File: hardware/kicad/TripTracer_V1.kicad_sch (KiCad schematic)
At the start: 0 parts

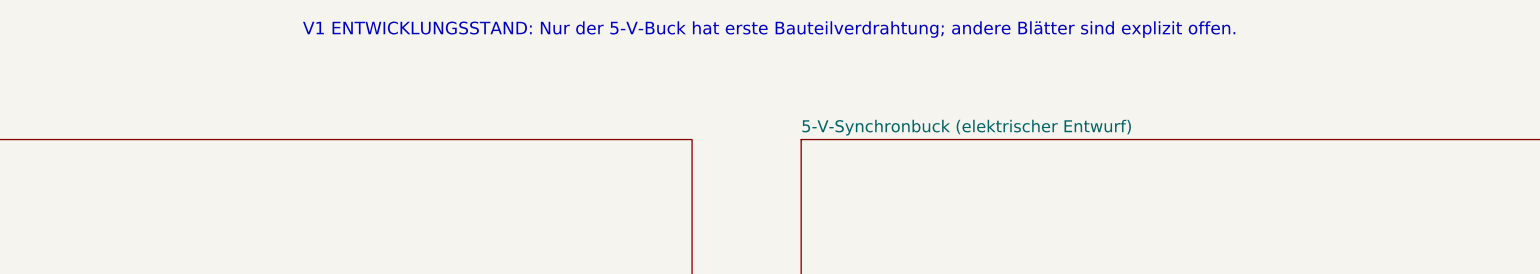
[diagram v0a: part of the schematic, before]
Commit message: hardware: mark V1 root with updated buck and MCU/USB implementation status
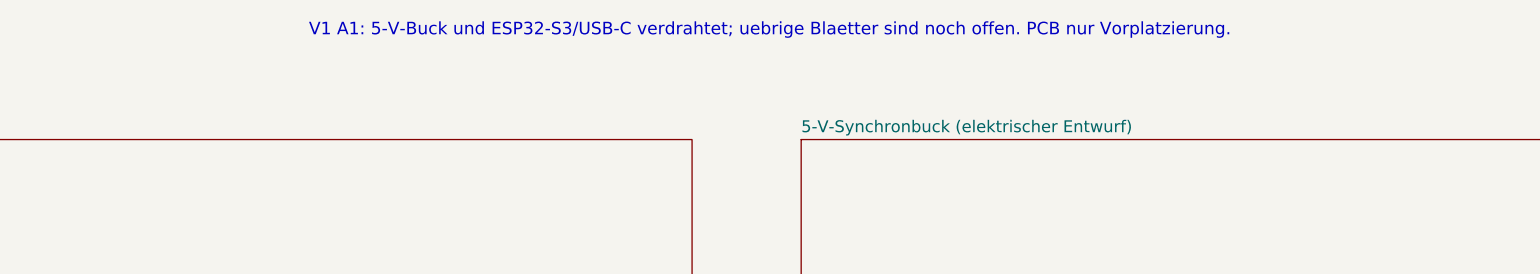
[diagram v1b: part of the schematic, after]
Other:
- note added: "V1 A1: 5-V-Buck und ESP32-S3/USB-C verdrahtet; uebrige Blaetter sind noch offen. PCB nur Vorplatzierung."
- note removed: "V1 ENTWICKLUNGSSTAND: Nur der 5-V-Buck hat erste Bauteilverdrahtung; andere Blätter sind explizit offen."
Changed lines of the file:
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@@
  (paper "A3")
  (title_block (title "TripTracer – Hardware V1 (Entwurf)") (date "2026-10-13") (rev "V1.0-a0 / NICHT FERTIGUNGSREIF") (company "TripTracer"))
- (text "V1 ENTWICKLUNGSSTAND: Nur der 5-V-Buck hat erste Bauteilverdrahtung; andere Blätter sind explizit offen." (at 210 16 0) (effects (font (size 1.6 1.6))))
+ (text "V1 A1: 5-V-Buck und ESP32-S3/USB-C verdrahtet; uebrige Blaetter sind noch offen. PCB nur Vorplatzierung." (at 210 16 0) (effects (font (size 1.6 1.6))))
  (sheet (at 25 30) (size 175 37) (exclude_from_sim no) (in_bom yes) (on_board yes) (dnp no)
  (stroke (width 0) (type solid)) (fill (color 0 0 0 0))

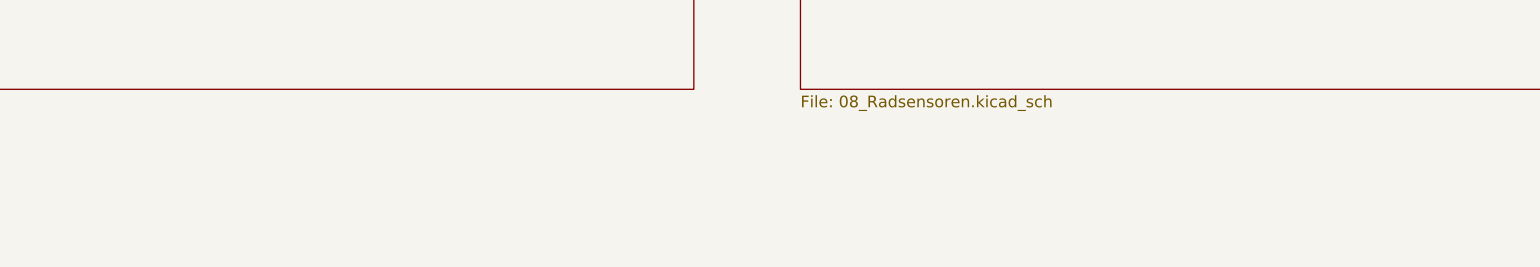
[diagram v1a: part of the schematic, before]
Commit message: hardware: annotate root schematic with single-project hierarchy navigation hint
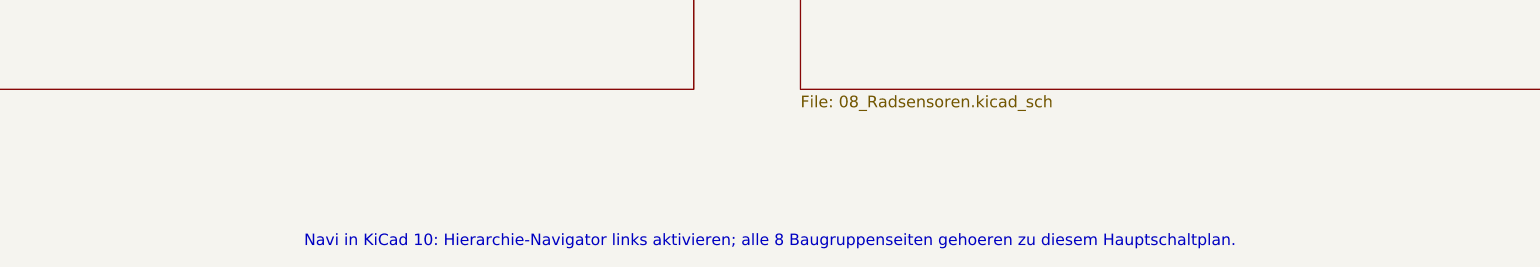
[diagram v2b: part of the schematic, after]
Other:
- note added: "Navi in KiCad 10: Hierarchie-Navigator links aktivieren; alle 8 Baugruppenseiten gehoeren zu diesem Hauptschaltplan."
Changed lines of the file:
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@@
  (property "Sheetfile" "08_Radsensoren.kicad_sch" (at 214 232.76 0) (effects (font (size 1.524 1.524)) (justify left top)))
  (instances (project "TripTracer_V1" (path "/a26d9b0c-7f10-4e5a-a65f-000000000064" (page "9")))))
+ (text "Navi in KiCad 10: Hierarchie-Navigator links aktivieren; alle 8 Baugruppenseiten gehoeren zu diesem Hauptschaltplan." (at 210 252 0) (effects (font (size 1.5 1.5))))
  (sheet_instances (path "/" (page "1")))
  (embedded_fonts no)

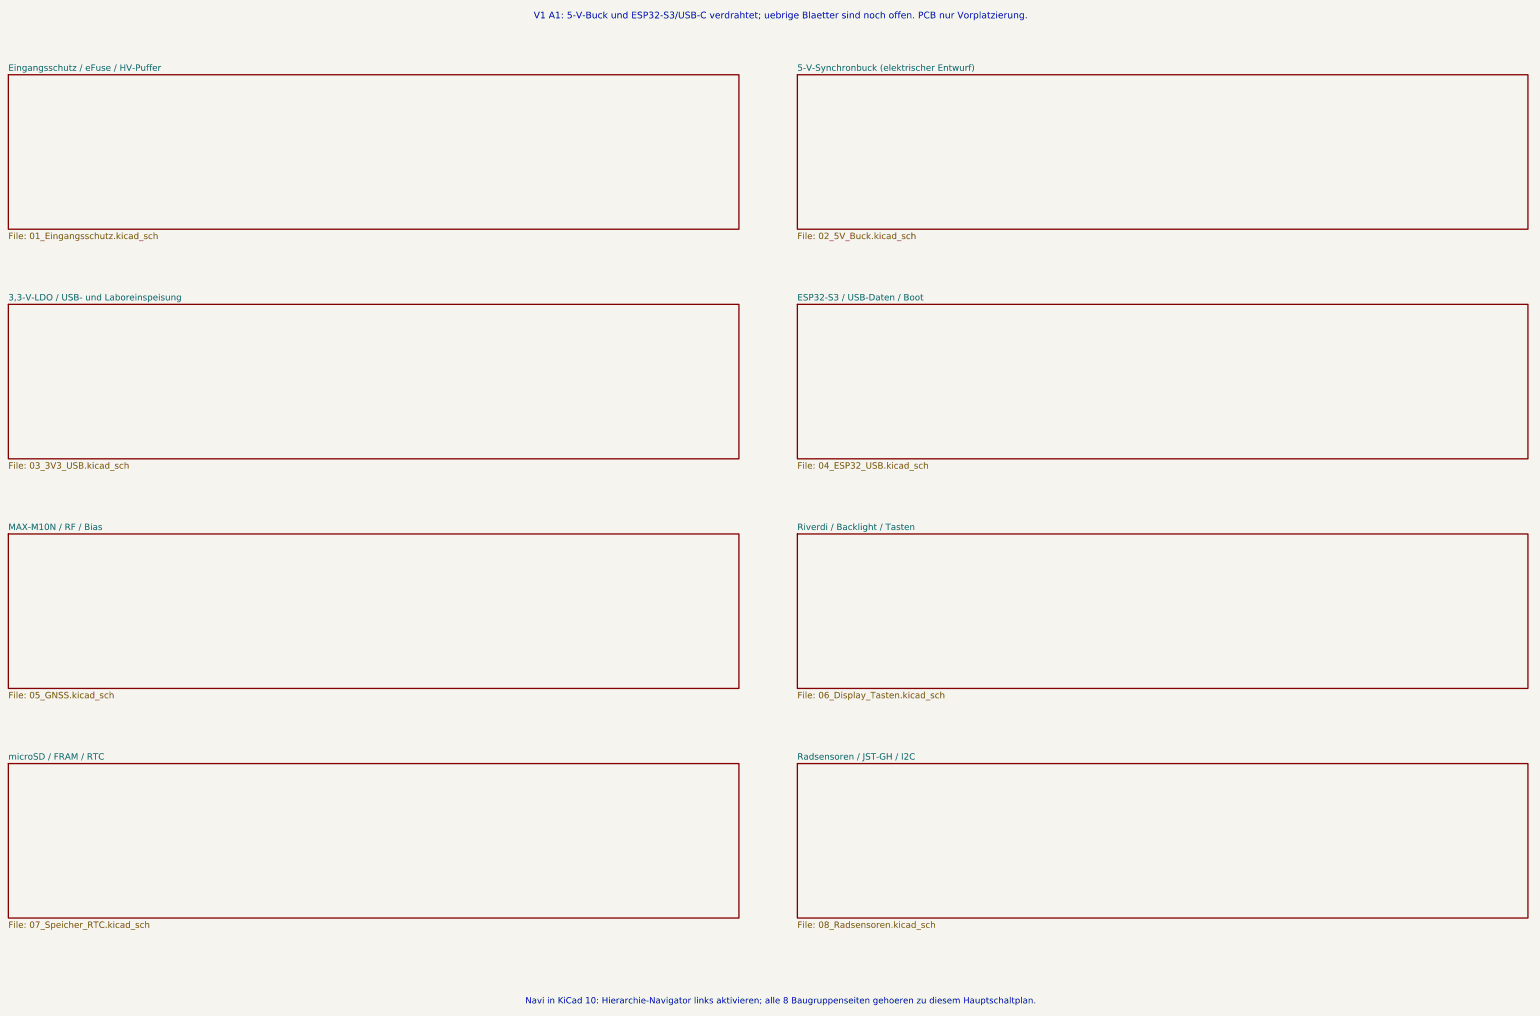
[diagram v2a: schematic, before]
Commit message: fix(kicad): align root hierarchy to connection grid without changing power nets
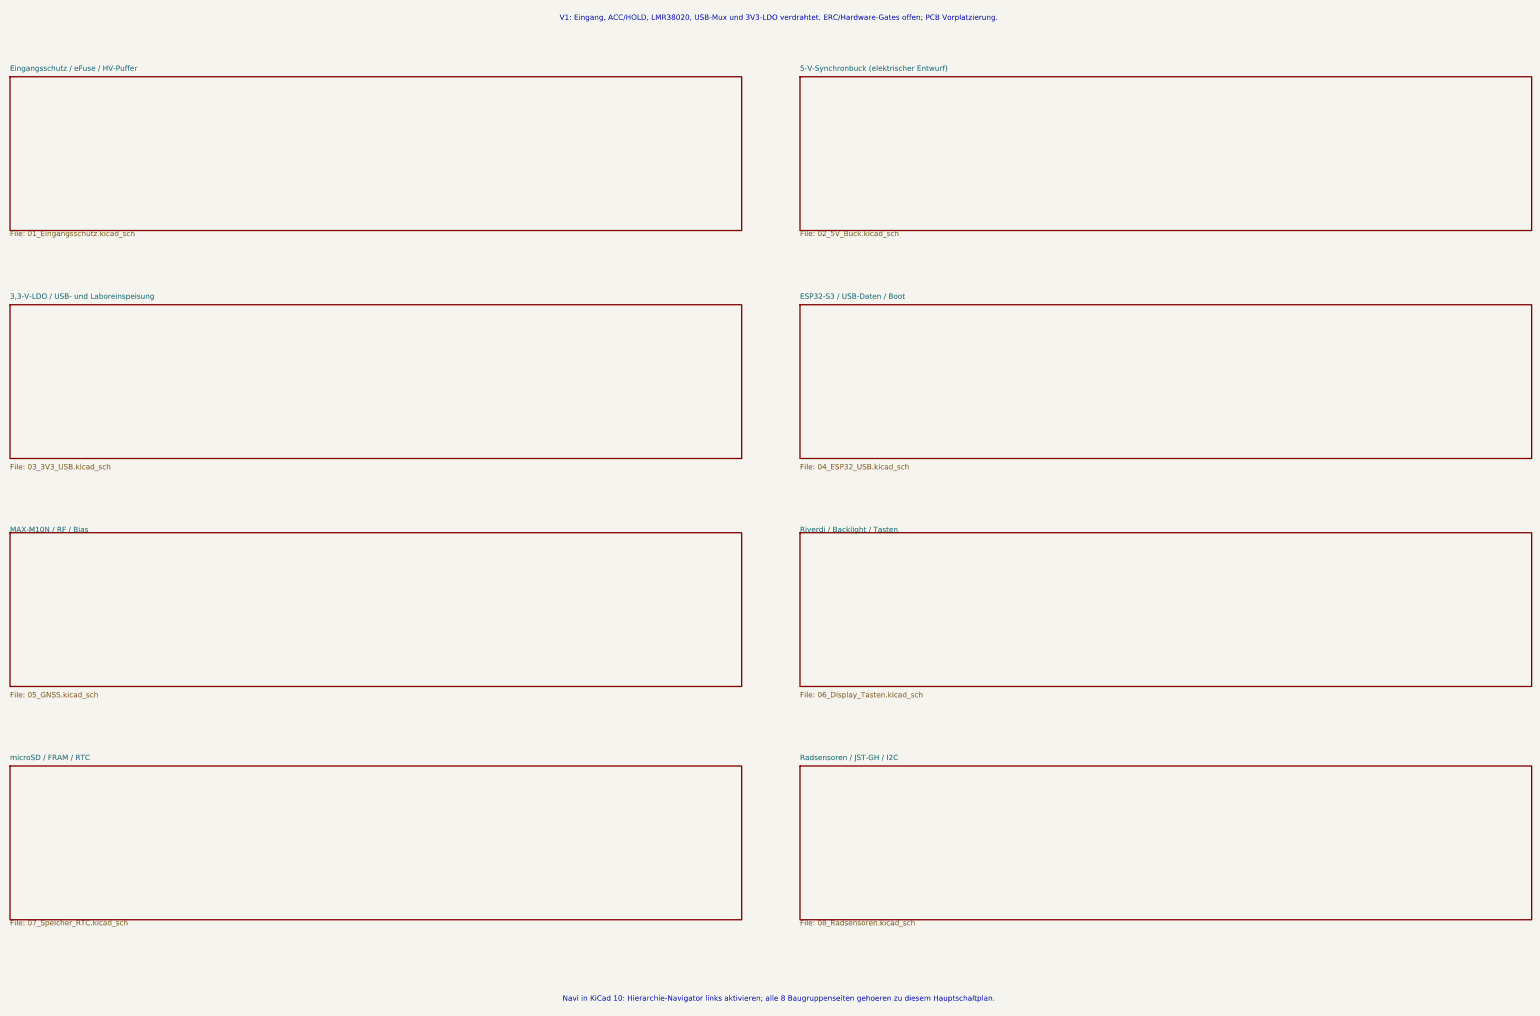
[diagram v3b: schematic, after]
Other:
- note added: "V1: Eingang, ACC/HOLD, LMR38020, USB-Mux und 3V3-LDO verdrahtet. ERC/Hardware-Gates offen; PCB Vorplatzierung."
- note removed: "V1 A1: 5-V-Buck und ESP32-S3/USB-C verdrahtet; uebrige Blaetter sind noch offen. PCB nur Vorplatzierung."
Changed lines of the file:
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@@
  (paper "A3")
  (title_block (title "TripTracer – Hardware V1 (Entwurf)") (date "2026-10-13") (rev "V1.0-a0 / NICHT FERTIGUNGSREIF") (company "TripTracer"))
- (text "V1 A1: 5-V-Buck und ESP32-S3/USB-C verdrahtet; uebrige Blaetter sind noch offen. PCB nur Vorplatzierung." (at 210 16 0) (effects (font (size 1.6 1.6))))
- (sheet (at 25 30) (size 175 37) (exclude_from_sim no) (in_bom yes) (on_board yes) (dnp no)
+ (text "V1: Eingang, ACC/HOLD, LMR38020, USB-Mux und 3V3-LDO verdrahtet. ERC/Hardware-Gates offen; PCB Vorplatzierung." (at 209.55 16.51 0) (effects (font (size 1.27 1.27))))
+ (sheet (at 25.4 30.48) (size 175.26 36.83) (exclude_from_sim no) (in_bom yes) (on_board yes) (dnp no)
  (stroke (width 0) (type solid)) (fill (color 0 0 0 0))
- (property "Sheetname" "Eingangsschutz / eFuse / HV-Puffer" (at 25 29.24 0) (effects (font (size 1.524 1.524)) (justify left bottom)))
- (property "Sheetfile" "01_Eingangsschutz.kicad_sch" (at 25 67.76 0) (effects (font (size 1.524 1.524)) (justify left top)))
+ (property "Sheetname" "Eingangsschutz / eFuse / HV-Puffer" (at 25.4 29.21 0) (effects (font (size 1.27 1.27)) (justify left bottom)))
+ (property "Sheetfile" "01_Eingangsschutz.kicad_sch" (at 25.4 67.31 0) (effects (font (size 1.27 1.27)) (justify left top)))
  (instances (project "TripTracer_V1" (path "/a26d9b0c-7f10-4e5a-a65f-000000000064" (page "2")))))
-(sheet (at 214 30) (size 175 37) (exclude_from_sim no) (in_bom yes) (on_board yes) (dnp no)
+(sheet (at 214.63 30.48) (size 175.26 36.83) (exclude_from_sim no) (in_bom yes) (on_board yes) (dnp no)
  (stroke (width 0) (type solid)) (fill (color 0 0 0 0))
- (property "Sheetname" "5-V-Synchronbuck (elektrischer Entwurf)" (at 214 29.24 0) (effects (font (size 1.524 1.524)) (justify left bottom)))
- (property "Sheetfile" "02_5V_Buck.kicad_sch" (at 214 67.76 0) (effects (font (size 1.524 1.524)) (justify left top)))
+ (property "Sheetname" "5-V-Synchronbuck (elektrischer Entwurf)" (at 214.63 29.21 0) (effects (font (size 1.27 1.27)) (justify left bottom)))
+ (property "Sheetfile" "02_5V_Buck.kicad_sch" (at 214.63 67.31 0) (effects (font (size 1.27 1.27)) (justify left top)))
  (instances (project "TripTracer_V1" (path "/a26d9b0c-7f10-4e5a-a65f-000000000064" (page "3")))))
-(sheet (at 25 85) (size 175 37) (exclude_from_sim no) (in_bom yes) (on_board yes) (dnp no)
+(sheet (at 25.4 85.09) (size 175.26 36.83) (exclude_from_sim no) (in_bom yes) (on_board yes) (dnp no)
  (stroke (width 0) (type solid)) (fill (color 0 0 0 0))
- (property "Sheetname" "3,3-V-LDO / USB- und Laboreinspeisung" (at 25 84.24 0) (effects (font (size 1.524 1.524)) (justify left bottom)))
- (property "Sheetfile" "03_3V3_USB.kicad_sch" (at 25 122.76 0) (effects (font (size 1.524 1.524)) (justify left top)))
+ (property "Sheetname" "3,3-V-LDO / USB- und Laboreinspeisung" (at 25.4 83.82 0) (effects (font (size 1.27 1.27)) (justify left bottom)))
+ (property "Sheetfile" "03_3V3_USB.kicad_sch" (at 25.4 123.19 0) (effects (font (size 1.27 1.27)) (justify left top)))
  (instances (project "TripTracer_V1" (path "/a26d9b0c-7f10-4e5a-a65f-000000000064" (page "4")))))
-(sheet (at 214 85) (size 175 37) (exclude_from_sim no) (in_bom yes) (on_board yes) (dnp no)
+(sheet (at 214.63 85.09) (size 175.26 36.83) (exclude_from_sim no) (in_bom yes) (on_board yes) (dnp no)
  (stroke (width 0) (type solid)) (fill (color 0 0 0 0))
- (property "Sheetname" "ESP32-S3 / USB-Daten / Boot" (at 214 84.24 0) (effects (font (size 1.524 1.524)) (justify left bottom)))
- (property "Sheetfile" "04_ESP32_USB.kicad_sch" (at 214 122.76 0) (effects (font (size 1.524 1.524)) (justify left top)))
+ (property "Sheetname" "ESP32-S3 / USB-Daten / Boot" (at 214.63 83.82 0) (effects (font (size 1.27 1.27)) (justify left bottom)))
+ (property "Sheetfile" "04_ESP32_USB.kicad_sch" (at 214.63 123.19 0) (effects (font (size 1.27 1.27)) (justify left top)))
  (instances (project "TripTracer_V1" (path "/a26d9b0c-7f10-4e5a-a65f-000000000064" (page "5")))))
-(sheet (at 25 140) (size 175 37) (exclude_from_sim no) (in_bom yes) (on_board yes) (dnp no)
+(sheet (at 25.4 139.7) (size 175.26 36.83) (exclude_from_sim no) (in_bom yes) (on_board yes) (dnp no)
  (stroke (width 0) (type solid)) (fill (color 0 0 0 0))
- (property "Sheetname" "MAX-M10N / RF / Bias" (at 25 139.24 0) (effects (font (size 1.524 1.524)) (justify left bottom)))
- (property "Sheetfile" "05_GNSS.kicad_sch" (at 25 177.76 0) (effects (font (size 1.524 1.524)) (justify left top)))
+ (property "Sheetname" "MAX-M10N / RF / Bias" (at 25.4 139.7 0) (effects (font (size 1.27 1.27)) (justify left bottom)))
+ (property "Sheetfile" "05_GNSS.kicad_sch" (at 25.4 177.8 0) (effects (font (size 1.27 1.27)) (justify left top)))
  (instances (project "TripTracer_V1" (path "/a26d9b0c-7f10-4e5a-a65f-000000000064" (page "6")))))
-(sheet (at 214 140) (size 175 37) (exclude_from_sim no) (in_bom yes) (on_board yes) (dnp no)
+(sheet (at 214.63 139.7) (size 175.26 36.83) (exclude_from_sim no) (in_bom yes) (on_board yes) (dnp no)
  (stroke (width 0) (type solid)) (fill (color 0 0 0 0))
- (property "Sheetname" "Riverdi / Backlight / Tasten" (at 214 139.24 0) (effects (font (size 1.524 1.524)) (justify left bottom)))
- (property "Sheetfile" "06_Display_Tasten.kicad_sch" (at 214 177.76 0) (effects (font (size 1.524 1.524)) (justify left top)))
+ (property "Sheetname" "Riverdi / Backlight / Tasten" (at 214.63 139.7 0) (effects (font (size 1.27 1.27)) (justify left bottom)))
+ (property "Sheetfile" "06_Display_Tasten.kicad_sch" (at 214.63 177.8 0) (effects (font (size 1.27 1.27)) (justify left top)))
  (instances (project "TripTracer_V1" (path "/a26d9b0c-7f10-4e5a-a65f-000000000064" (page "7")))))
-(sheet (at 25 195) (size 175 37) (exclude_from_sim no) (in_bom yes) (on_board yes) (dnp no)
+(sheet (at 25.4 195.58) (size 175.26 36.83) (exclude_from_sim no) (in_bom yes) (on_board yes) (dnp no)
  (stroke (width 0) (type solid)) (fill (color 0 0 0 0))
- (property "Sheetname" "microSD / FRAM / RTC" (at 25 194.24 0) (effects (font (size 1.524 1.524)) (justify left bottom)))
- (property "Sheetfile" "07_Speicher_RTC.kicad_sch" (at 25 232.76 0) (effects (font (size 1.524 1.524)) (justify left top)))
+ (property "Sheetname" "microSD / FRAM / RTC" (at 25.4 194.31 0) (effects (font (size 1.27 1.27)) (justify left bottom)))
+ (property "Sheetfile" "07_Speicher_RTC.kicad_sch" (at 25.4 232.41 0) (effects (font (size 1.27 1.27)) (justify left top)))
  (instances (project "TripTracer_V1" (path "/a26d9b0c-7f10-4e5a-a65f-000000000064" (page "8")))))
-(sheet (at 214 195) (size 175 37) (exclude_from_sim no) (in_bom yes) (on_board yes) (dnp no)
+(sheet (at 214.63 195.58) (size 175.26 36.83) (exclude_from_sim no) (in_bom yes) (on_board yes) (dnp no)
  (stroke (width 0) (type solid)) (fill (color 0 0 0 0))
- (property "Sheetname" "Radsensoren / JST-GH / I2C" (at 214 194.24 0) (effects (font (size 1.524 1.524)) (justify left bottom)))
- (property "Sheetfile" "08_Radsensoren.kicad_sch" (at 214 232.76 0) (effects (font (size 1.524 1.524)) (justify left top)))
+ (property "Sheetname" "Radsensoren / JST-GH / I2C" (at 214.63 194.31 0) (effects (font (size 1.27 1.27)) (justify left bottom)))
+ (property "Sheetfile" "08_Radsensoren.kicad_sch" (at 214.63 232.41 0) (effects (font (size 1.27 1.27)) (justify left top)))
  (instances (project "TripTracer_V1" (path "/a26d9b0c-7f10-4e5a-a65f-000000000064" (page "9")))))
- (text "Navi in KiCad 10: Hierarchie-Navigator links aktivieren; alle 8 Baugruppenseiten gehoeren zu diesem Hauptschaltplan." (at 210 252 0) (effects (font (size 1.5 1.5))))
+ (text "Navi in KiCad 10: Hierarchie-Navigator links aktivieren; alle 8 Baugruppenseiten gehoeren zu diesem Hauptschaltplan." (at 209.55 251.46 0) (effects (font (size 1.27 1.27))))
  (sheet_instances (path "/" (page "1")))
  (embedded_fonts no)
